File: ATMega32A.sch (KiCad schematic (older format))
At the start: 18 parts, among them J301 UART, J302 AVR-ISP-6, U301 ATmega32A-AU, Y301 16MHz

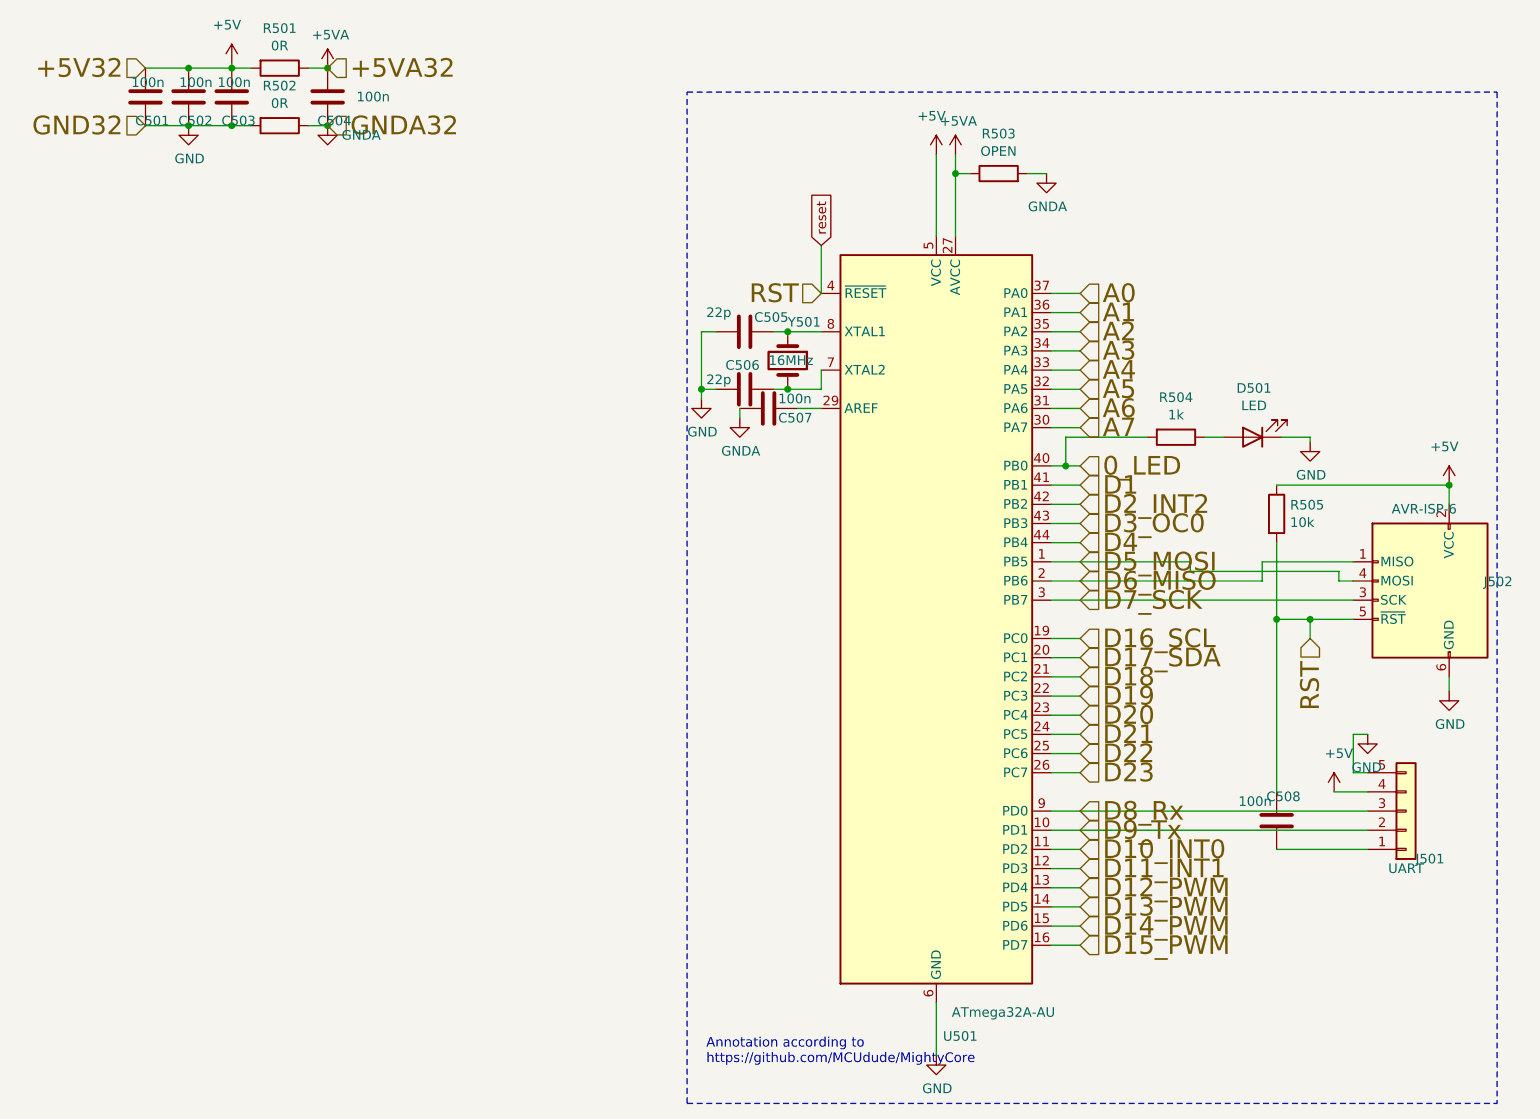
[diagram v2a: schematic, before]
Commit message: D1 -> D1_DAC
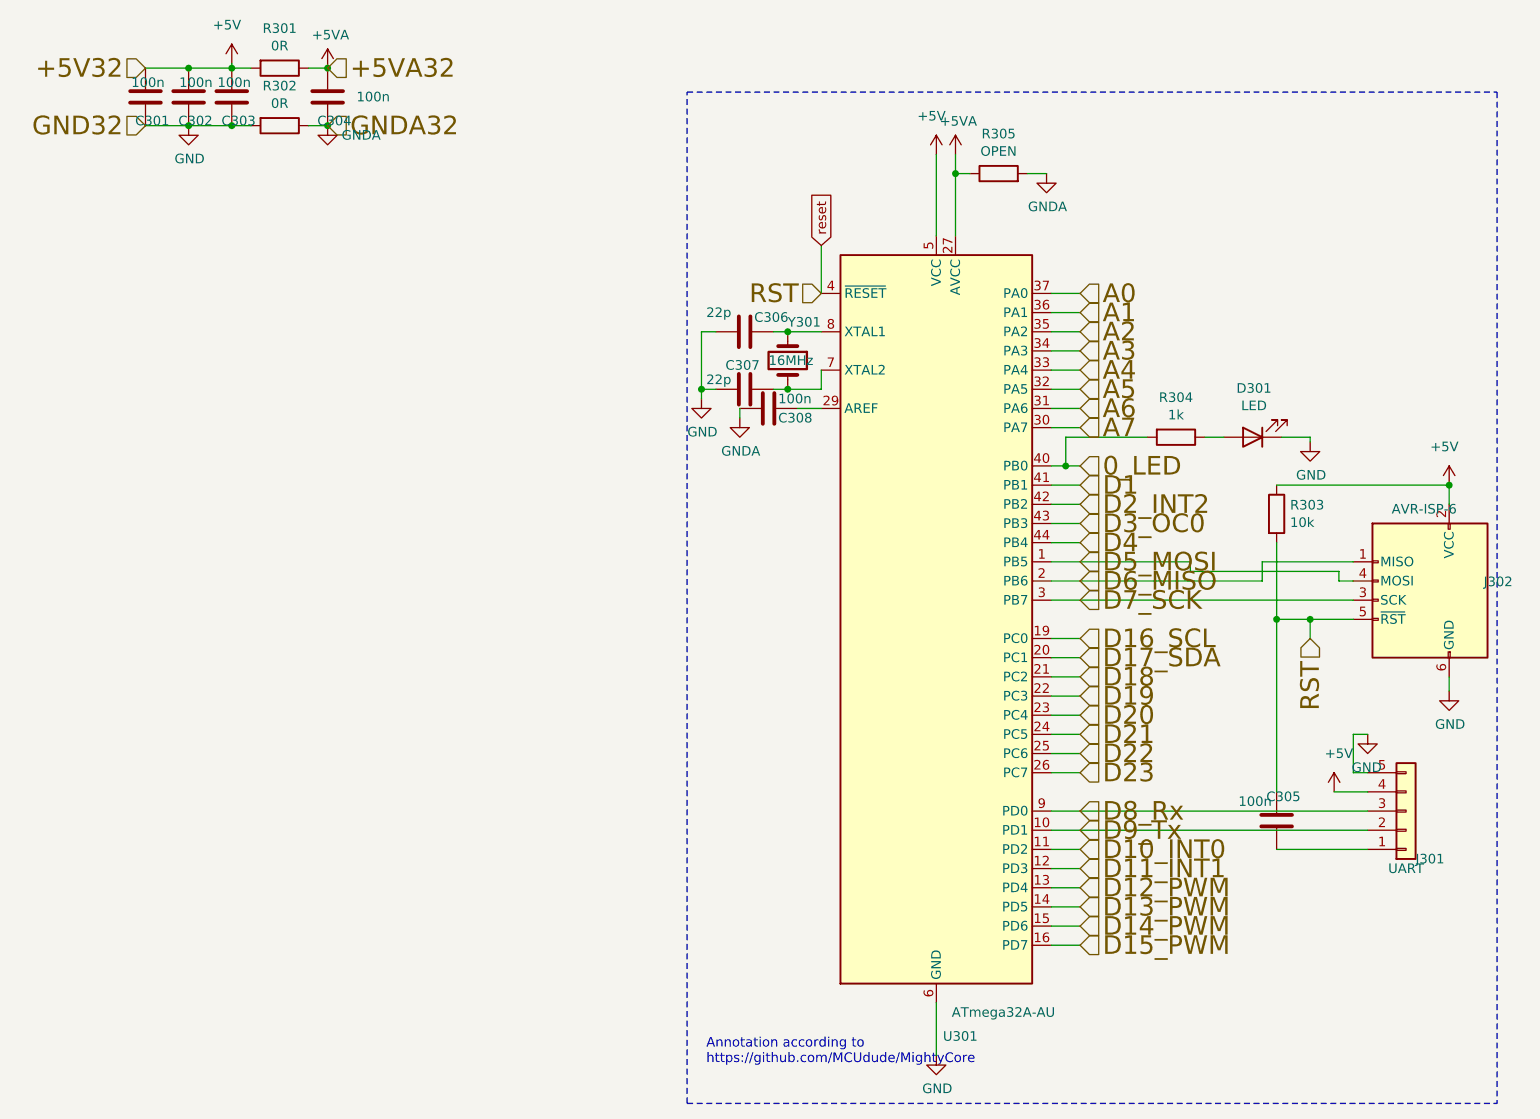
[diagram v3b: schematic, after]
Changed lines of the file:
@@
 $Descr A4 11693 8268
 encoding utf-8
-Sheet 5 5
+Sheet 3 5
 Title "Kicad_JE_ADSR_Mega32"
 Date "2019-05-13"
@@
 AR Path="/623B09EB/5CD3F059/5CD50179" Ref="U?"  Part="1"
 AR Path="/623B09EB/6241086C/5CD50179" Ref="U501"  Part="1"
-F 0 "U501" H 6300 1550 50  0000 C CNN
+F 0 "U301" H 6300 1550 50  0000 C CNN
 F 1 "ATmega32A-AU" H 6525 1675 50  0000 C CNN
 F 2 "Package_QFP:TQFP-44_10x10mm_P0.8mm" H 6175 3725 50  0001 C CIN
@@
 AR Path="/623B09EB/5CD3F059/5CD5017F" Ref="J?"  Part="1"
 AR Path="/623B09EB/6241086C/5CD5017F" Ref="J502"  Part="1"
-F 0 "J502" H 8470 3721 50  0000 R CNN
+F 0 "J302" H 8470 3721 50  0000 R CNN
 F 1 "AVR-ISP-6" H 8950 4100 50  0000 R CNN
 F 2 "Connector_PinHeader_2.54mm:PinHeader_2x03_P2.54mm_Vertical" V 8500 3675 50  0001 C CNN
@@
 AR Path="/623B09EB/5CD3F059/5CD50185" Ref="J?"  Part="1"
 AR Path="/623B09EB/6241086C/5CD50185" Ref="J501"  Part="1"
-F 0 "J501" H 8750 4975 50  0000 C CNN
+F 0 "J301" H 8750 4975 50  0000 C CNN
 F 1 "UART" H 8625 5025 50  0000 C CNN
 F 2 "Connector_PinHeader_2.54mm:PinHeader_1x05_P2.54mm_Vertical" H 8625 4725 50  0001 C CNN
@@
 AR Path="/623B09EB/5CD3F059/5CD5019E" Ref="C?"  Part="1"
 AR Path="/623B09EB/6241086C/5CD5019E" Ref="C508"  Part="1"
-F 0 "C508" H 7825 4900 50  0000 L CNN
+F 0 "C305" H 7825 4900 50  0000 L CNN
 F 1 "100n" H 7975 4875 50  0000 L CNN
 F 2 "AJ:C_0805_AJ" H 7988 4625 50  0001 C CNN
@@
 AR Path="/623B09EB/5CD3F059/5CD501A6" Ref="R?"  Part="1"
 AR Path="/623B09EB/6241086C/5CD501A6" Ref="R505"  Part="1"
-F 0 "R505" H 8020 3221 50  0000 L CNN
+F 0 "R303" H 8020 3221 50  0000 L CNN
 F 1 "10k" H 8020 3130 50  0000 L CNN
 F 2 "AJ:R_0805_AJ" V 7880 3175 50  0001 C CNN
@@
 AR Path="/623B09EB/5CD3F059/5CD501CD" Ref="Y?"  Part="1"
 AR Path="/623B09EB/6241086C/5CD501CD" Ref="Y501"  Part="1"
-F 0 "Y501" V 5200 2375 50  0000 L CNN
+F 0 "Y301" V 5200 2375 50  0000 L CNN
 F 1 "16MHz" V 5400 2275 50  0000 L CNN
 F 2 "Crystal:Crystal_HC49-U_Vertical" H 5400 2375 50  0001 C CNN
@@
 AR Path="/623B09EB/5CD3F059/5CD501D9" Ref="C?"  Part="1"
 AR Path="/623B09EB/6241086C/5CD501D9" Ref="C506"  Part="1"
-F 0 "C506" V 5050 2425 50  0000 L CNN
+F 0 "C307" V 5050 2425 50  0000 L CNN
 F 1 "22p" V 5125 2325 50  0000 L CNN
 F 2 "AJ:C_0805_AJ" H 5213 2375 50  0001 C CNN
@@
 AR Path="/623B09EB/5CD3F059/5CD501E0" Ref="C?"  Part="1"
 AR Path="/623B09EB/6241086C/5CD501E0" Ref="C505"  Part="1"
-F 0 "C505" V 5100 2275 50  0000 L CNN
+F 0 "C306" V 5100 2275 50  0000 L CNN
 F 1 "22p" V 5075 2025 50  0000 L CNN
 F 2 "AJ:C_0805_AJ" H 5213 2075 50  0001 C CNN
@@
 AR Path="/623B09EB/5CD3F059/5CD501E9" Ref="#PWR?"  Part="1"
 AR Path="/623B09EB/6241086C/5CD501E9" Ref="#PWR0510"  Part="1"
-F 0 "#PWR0510" H 6750 1150 50  0001 C CNN
+F 0 "#PWR0128" H 6750 1150 50  0001 C CNN
 F 1 "GNDA" H 6755 1227 50  0000 C CNN
 F 2 "" H 6750 1400 50  0001 C CNN
@@
 AR Path="/623B09EB/5CD3F059/5CD501EF" Ref="#PWR?"  Part="1"
 AR Path="/623B09EB/6241086C/5CD501EF" Ref="#PWR0506"  Part="1"
-F 0 "#PWR0506" H 5150 2425 50  0001 C CNN
+F 0 "#PWR0129" H 5150 2425 50  0001 C CNN
 F 1 "GNDA" H 5155 2502 50  0000 C CNN
 F 2 "" H 5150 2675 50  0001 C CNN
@@
 AR Path="/623B09EB/5CD3F059/5CD501F7" Ref="R?"  Part="1"
 AR Path="/623B09EB/6241086C/5CD501F7" Ref="R504"  Part="1"
-F 0 "R504" V 7218 2775 50  0000 C CNN
+F 0 "R304" V 7218 2775 50  0000 C CNN
 F 1 "1k" V 7309 2775 50  0000 C CNN
 F 2 "AJ:R_0805_AJ" V 7355 2775 50  0001 C CNN
@@
 AR Path="/623B09EB/5CD3F059/5CD501FD" Ref="D?"  Part="1"
 AR Path="/623B09EB/6241086C/5CD501FD" Ref="D501"  Part="1"
-F 0 "D501" H 7818 2520 50  0000 C CNN
+F 0 "D301" H 7818 2520 50  0000 C CNN
 F 1 "LED" H 7818 2611 50  0000 C CNN
 F 2 "AJ:D_0805_AJ" H 7825 2775 50  0001 C CNN
@@
 AR Path="/623B09EB/5CD3F059/5CD5023A" Ref="R?"  Part="1"
 AR Path="/623B09EB/6241086C/5CD5023A" Ref="R503"  Part="1"
-F 0 "R503" V 6707 1400 50  0000 C CNN
+F 0 "R305" V 6707 1400 50  0000 C CNN
 F 1 "OPEN" V 6616 1400 50  0000 C CNN
 F 2 "AJ:R_0805_AJ" V 6430 1400 50  0001 C CNN
@@
 AR Path="/623B09EB/5CD3F059/5CD5024D" Ref="#PWR?"  Part="1"
 AR Path="/623B09EB/6241086C/5CD5024D" Ref="#PWR0509"  Part="1"
-F 0 "#PWR0509" H 6275 1150 50  0001 C CNN
+F 0 "#PWR0130" H 6275 1150 50  0001 C CNN
 F 1 "+5VA" H 6290 1473 50  0000 C CNN
 F 2 "" H 6275 1300 50  0001 C CNN
@@
 AR Path="/623B09EB/5CD3F059/5CD5760D" Ref="R?"  Part="1"
 AR Path="/623B09EB/6241086C/5CD5760D" Ref="R501"  Part="1"
-F 0 "R501" V 2543 850 50  0000 C CNN
+F 0 "R301" V 2543 850 50  0000 C CNN
 F 1 "0R" V 2634 850 50  0000 C CNN
 F 2 "AJ:R_0805_AJ" V 2680 850 50  0001 C CNN
@@
 AR Path="/623B09EB/5CD3F059/5CD57617" Ref="#PWR?"  Part="1"
 AR Path="/623B09EB/6241086C/5CD57617" Ref="#PWR0503"  Part="1"
-F 0 "#PWR0503" H 3000 700 50  0001 C CNN
+F 0 "#PWR0131" H 3000 700 50  0001 C CNN
 F 1 "+5VA" H 3015 1023 50  0000 C CNN
 F 2 "" H 3000 850 50  0001 C CNN
@@
 AR Path="/623B09EB/5CD3F059/5CD5761D" Ref="C?"  Part="1"
 AR Path="/623B09EB/6241086C/5CD5761D" Ref="C504"  Part="1"
-F 0 "C504" H 2875 1125 50  0000 L CNN
+F 0 "C304" H 2875 1125 50  0000 L CNN
 F 1 "100n" H 2675 1000 50  0000 L CNN
 F 2 "AJ:C_0805_AJ" H 3038 850 50  0001 C CNN
@@
 AR Path="/623B09EB/5CD3F059/5CD57623" Ref="C?"  Part="1"
 AR Path="/623B09EB/6241086C/5CD57623" Ref="C503"  Part="1"
-F 0 "C503" H 2375 1125 50  0000 L CNN
+F 0 "C303" H 2375 1125 50  0000 L CNN
 F 1 "100n" H 2400 925 50  0000 L CNN
 F 2 "AJ:C_0805_AJ" H 2538 850 50  0001 C CNN
@@
 AR Path="/623B09EB/5CD3F059/5CD5762A" Ref="C?"  Part="1"
 AR Path="/623B09EB/6241086C/5CD5762A" Ref="C502"  Part="1"
-F 0 "C502" H 2150 1125 50  0000 L CNN
+F 0 "C302" H 2150 1125 50  0000 L CNN
 F 1 "100n" H 2150 925 50  0000 L CNN
 F 2 "AJ:C_0805_AJ" H 2313 850 50  0001 C CNN
@@
 AR Path="/623B09EB/5CD3F059/5CD57630" Ref="C?"  Part="1"
 AR Path="/623B09EB/6241086C/5CD57630" Ref="C501"  Part="1"
-F 0 "C501" H 1925 1125 50  0000 L CNN
+F 0 "C301" H 1925 1125 50  0000 L CNN
 F 1 "100n" H 1950 925 50  0000 L CNN
 F 2 "AJ:C_0805_AJ" H 2088 850 50  0001 C CNN
@@
 AR Path="/623B09EB/5CD3F059/5CD5763C" Ref="#PWR?"  Part="1"
 AR Path="/623B09EB/6241086C/5CD5763C" Ref="#PWR0504"  Part="1"
-F 0 "#PWR0504" H 3000 900 50  0001 C CNN
+F 0 "#PWR0132" H 3000 900 50  0001 C CNN
 F 1 "GNDA" H 3175 1100 50  0000 C CNN
 F 2 "" H 3000 1150 50  0001 C CNN
@@
 AR Path="/623B09EB/5CD3F059/5CD57648" Ref="R?"  Part="1"
 AR Path="/623B09EB/6241086C/5CD57648" Ref="R502"  Part="1"
-F 0 "R502" V 2543 1150 50  0000 C CNN
+F 0 "R302" V 2543 1150 50  0000 C CNN
 F 1 "0R" V 2634 1150 50  0000 C CNN
 F 2 "Jumper:SolderJumper-2_P1.3mm_Bridged_RoundedPad1.0x1.5mm" V 2680 1150 50  0001 C CNN
@@
 AR Path="/623B09EB/5CD3F059/609C19AF" Ref="#PWR?"  Part="1"
 AR Path="/623B09EB/6241086C/609C19AF" Ref="#PWR0502"  Part="1"
-F 0 "#PWR0502" H 2500 675 50  0001 C CNN
+F 0 "#PWR0133" H 2500 675 50  0001 C CNN
 F 1 "+5V" H 2475 1025 50  0000 C CNN
 F 2 "" H 2500 825 50  0001 C CNN
@@
 AR Path="/623B09EB/5CD3F059/609DD6C9" Ref="#PWR?"  Part="1"
 AR Path="/623B09EB/6241086C/609DD6C9" Ref="#PWR0501"  Part="1"
-F 0 "#PWR0501" H 2275 900 50  0001 C CNN
+F 0 "#PWR0134" H 2275 900 50  0001 C CNN
 F 1 "GND" H 2280 977 50  0000 C CNN
 F 2 "" H 2275 1150 50  0001 C CNN
@@
 AR Path="/623B09EB/5CD3F059/609DDA2F" Ref="#PWR?"  Part="1"
 AR Path="/623B09EB/6241086C/609DDA2F" Ref="#PWR0505"  Part="1"
-F 0 "#PWR0505" H 4950 2325 50  0001 C CNN
+F 0 "#PWR0135" H 4950 2325 50  0001 C CNN
 F 1 "GND" H 4955 2402 50  0000 C CNN
 F 2 "" H 4950 2575 50  0001 C CNN
@@
 AR Path="/623B09EB/5CD3F059/609DE081" Ref="#PWR?"  Part="1"
 AR Path="/623B09EB/6241086C/609DE081" Ref="#PWR0511"  Part="1"
-F 0 "#PWR0511" H 8125 2550 50  0001 C CNN
+F 0 "#PWR0136" H 8125 2550 50  0001 C CNN
 F 1 "GND" H 8130 2627 50  0000 C CNN
 F 2 "" H 8125 2800 50  0001 C CNN
@@
 AR Path="/623B09EB/5CD3F059/609DE4CB" Ref="#PWR?"  Part="1"
 AR Path="/623B09EB/6241086C/609DE4CB" Ref="#PWR0515"  Part="1"
-F 0 "#PWR0515" H 8850 3850 50  0001 C CNN
+F 0 "#PWR0137" H 8850 3850 50  0001 C CNN
 F 1 "GND" H 8855 3927 50  0000 C CNN
 F 2 "" H 8850 4100 50  0001 C CNN
@@
 AR Path="/623B09EB/5CD3F059/609DE834" Ref="#PWR?"  Part="1"
 AR Path="/623B09EB/6241086C/609DE834" Ref="#PWR0513"  Part="1"
-F 0 "#PWR0513" H 8425 4075 50  0001 C CNN
+F 0 "#PWR0138" H 8425 4075 50  0001 C CNN
 F 1 "GND" H 8430 4152 50  0000 C CNN
 F 2 "" H 8425 4325 50  0001 C CNN
@@
 AR Path="/623B09EB/5CD3F059/609DEBD0" Ref="#PWR?"  Part="1"
 AR Path="/623B09EB/6241086C/609DEBD0" Ref="#PWR0508"  Part="1"
-F 0 "#PWR0508" H 6175 5750 50  0001 C CNN
+F 0 "#PWR0139" H 6175 5750 50  0001 C CNN
 F 1 "GND" H 6180 5827 50  0000 C CNN
 F 2 "" H 6175 6000 50  0001 C CNN
@@
 AR Path="/623B09EB/5CD3F059/60A08EFF" Ref="#PWR?"  Part="1"
 AR Path="/623B09EB/6241086C/60A08EFF" Ref="#PWR0514"  Part="1"
-F 0 "#PWR0514" H 8850 2875 50  0001 C CNN
+F 0 "#PWR0140" H 8850 2875 50  0001 C CNN
 F 1 "+5V" H 8825 3225 50  0000 C CNN
 F 2 "" H 8850 3025 50  0001 C CNN
@@
 AR Path="/623B09EB/5CD3F059/60A098C8" Ref="#PWR?"  Part="1"
 AR Path="/623B09EB/6241086C/60A098C8" Ref="#PWR0512"  Part="1"
-F 0 "#PWR0512" H 8250 4475 50  0001 C CNN
+F 0 "#PWR0141" H 8250 4475 50  0001 C CNN
 F 1 "+5V" H 8225 4825 50  0000 C CNN
 F 2 "" H 8250 4625 50  0001 C CNN
@@
 AR Path="/623B09EB/5CD3F059/60A42364" Ref="#PWR?"  Part="1"
 AR Path="/623B09EB/6241086C/60A42364" Ref="#PWR0507"  Part="1"
-F 0 "#PWR0507" H 6175 1150 50  0001 C CNN
+F 0 "#PWR0142" H 6175 1150 50  0001 C CNN
 F 1 "+5V" H 6150 1500 50  0000 C CNN
 F 2 "" H 6175 1300 50  0001 C CNN
@@
 AR Path="/623B09EB/5CD3F059/60A4BD33" Ref="C?"  Part="1"
 AR Path="/623B09EB/6241086C/60A4BD33" Ref="C507"  Part="1"
-F 0 "C507" V 5350 2675 50  0000 L CNN
+F 0 "C308" V 5350 2675 50  0000 L CNN
 F 1 "100n" V 5250 2675 50  0000 L CNN
 F 2 "AJ:C_0805_AJ" H 5338 2475 50  0001 C CNN
